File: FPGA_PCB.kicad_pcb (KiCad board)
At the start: 2 copper layers, 177.8 x 127 mm, 29 parts, among them J1 Conn_01x01_Male, J10 Conn_Coaxial, J11 Conn_Coaxial, J12 Conn_01x03_Male, J13 Conn_01x03_Male, J14 Conn_01x01_Male, J15 Conn_01x01_Male, J16 73096-2, J17 73096-2, J18 Conn_01x01_Male, J19 Conn_01x01_Male, J2 Conn_01x01_Male, J20 Conn_01x01_Male, J3 73096-2, J4 73096-2, J5 Conn_01x04_Male, J6 Conn_01x04_Male, J7 Conn_01x04_Male, J8 Conn_01x04_Male, J9 Conn_01x04_Male, SW1 SW_Push, U1 CPG08462

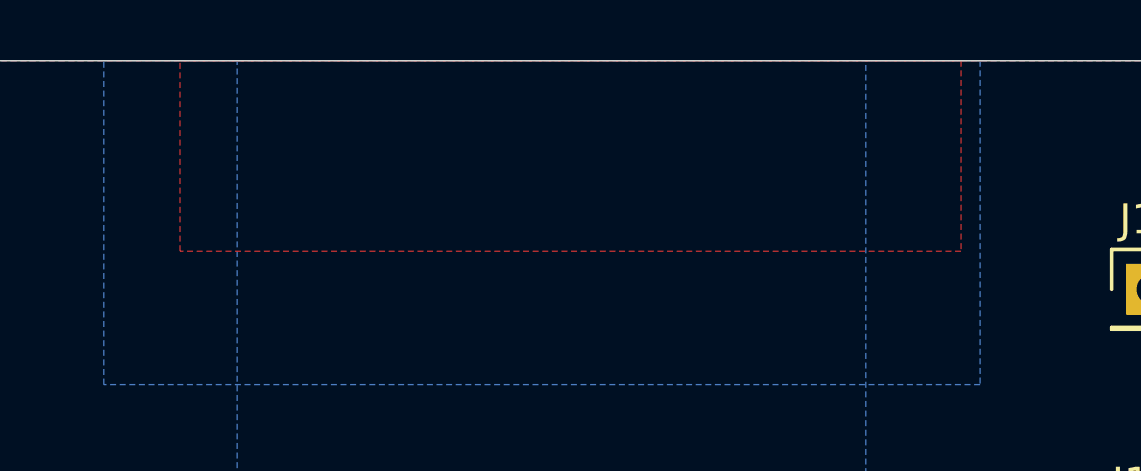
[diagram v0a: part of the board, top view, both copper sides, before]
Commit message: layout DRC fixed
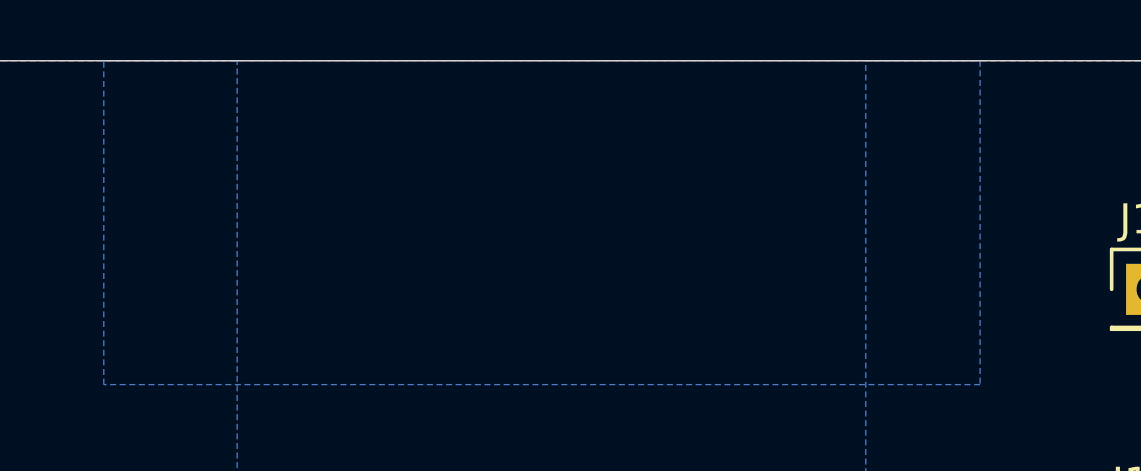
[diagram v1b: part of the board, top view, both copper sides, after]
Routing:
- removed copper zone on F.Cu, net /VSS
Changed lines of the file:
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@@
-    )
-  )
-  (zone (net 2) (net_name /VSS) (layer F.Cu) (hatch edge 0.508)
-    (connect_pads (clearance 0.508))
-    (min_thickness 0.254)
-    (fill yes (arc_segments 32) (thermal_gap 0.508) (thermal_bridge_width 0.508))
-    (polygon
-      (pts
-        (xy 109.855 25.4) (xy 135.89 25.4) (xy 135.89 31.75) (xy 109.855 31.75)
-      )
     )
   )
